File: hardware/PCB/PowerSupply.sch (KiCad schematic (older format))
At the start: 8 parts

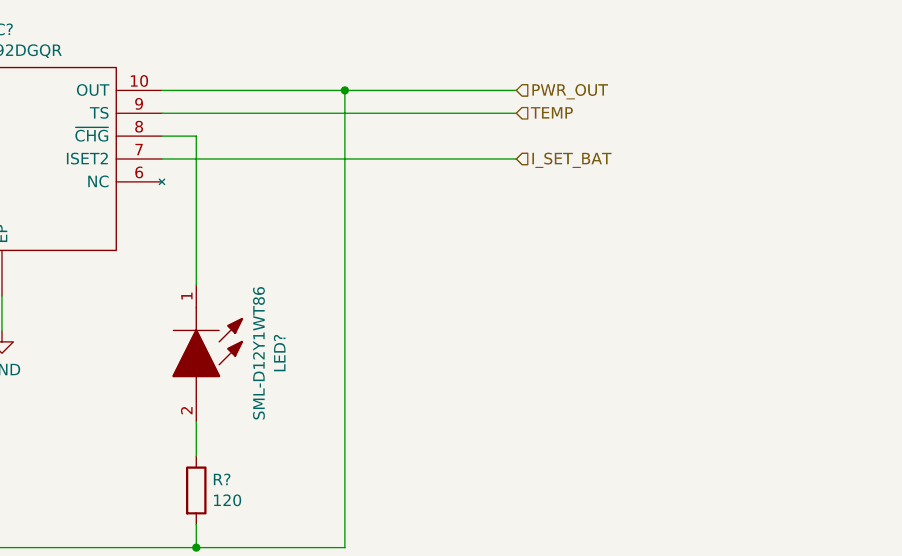
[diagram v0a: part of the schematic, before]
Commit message: Added battery connector
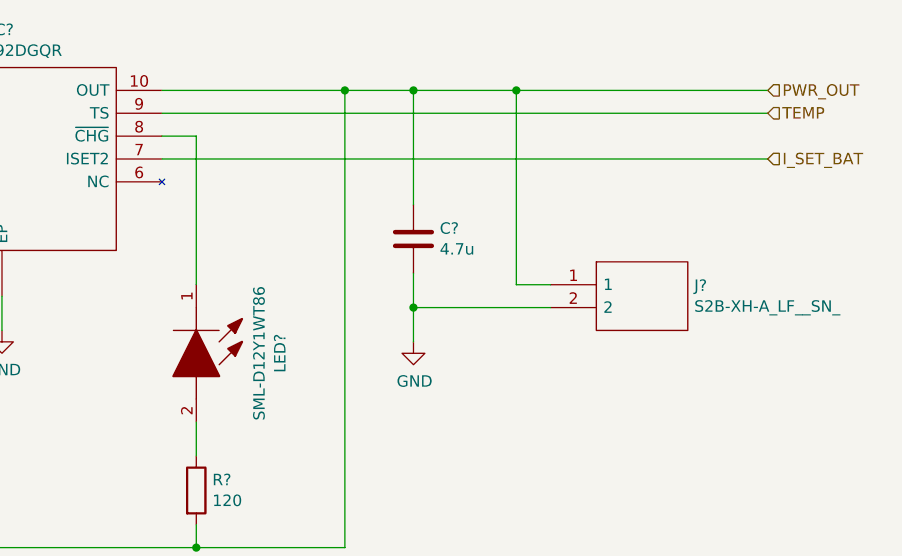
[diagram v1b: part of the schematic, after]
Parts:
- added C?: 4.7u, Capacitor_SMD:C_0603_1608Metric, symbol Device:C
- added J?: S2B-XH-A_LF__SN_, SHDRRA2W80P0X250_1X2_740X1150X610P, symbol ProjectLibrary:S2B-XH-A_LF__SN_
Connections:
- net GND: now also C?.2, J?.2
- net PWR_OUT: now also C?.1, J?.1
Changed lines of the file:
@@
 	1    0    0    -1
 $EndComp
-Text HLabel 6200 1650 2    50   Input ~ 0
+Text HLabel 7300 1650 2    50   Input ~ 0
 I_SET_BAT
-Text HLabel 6200 1450 2    50   Input ~ 0
+Text HLabel 7300 1450 2    50   Input ~ 0
 TEMP
 Wire Wire Line
@@
 Wire Wire Line
 	4650 1550 4800 1550
-Text HLabel 6200 1350 2    50   Input ~ 0
+Text HLabel 7300 1350 2    50   Input ~ 0
 PWR_OUT
 $Comp
@@
 Connection ~ 5450 1350
 Wire Wire Line
-	5450 1350 6200 1350
+	5450 1350 5750 1350
 Wire Wire Line
 	4650 1350 5450 1350
-Wire Wire Line
-	4650 1450 6200 1450
-Wire Wire Line
-	4650 1650 6200 1650
 Wire Wire Line
 	3150 2200 3150 1750
@@
 Wire Wire Line
 	3950 2250 3950 2400
+$Comp
+L Device:C C?
+U 1 1 5FC2DE09
+P 5750 2000
+F 0 "C?" H 5865 2046 50  0000 L CNN
+F 1 "4.7u" H 5865 1955 50  0000 L CNN
+F 2 "Capacitor_SMD:C_0603_1608Metric" H 5788 1850 50  0001 C CNN
+F 3 "~" H 5750 2000 50  0001 C CNN
+	1    5750 2000
+	1    0    0    -1
+$EndComp
+$Comp
+L power:GND #PWR?
+U 1 1 5FC2E9CD
+P 5750 2450
+F 0 "#PWR?" H 5750 2200 50  0001 C CNN
+F 1 "GND" H 5755 2277 50  0000 C CNN
+F 2 "" H 5750 2450 50  0001 C CNN
+F 3 "" H 5750 2450 50  0001 C CNN
+	1    5750 2450
+	1    0    0    -1
+$EndComp
+Wire Wire Line
+	5750 2300 5750 2150
+Wire Wire Line
+	5750 1850 5750 1350
+Connection ~ 5750 1350
+Wire Wire Line
+	5750 1350 6200 1350
+$Comp
+L ProjectLibrary:S2B-XH-A_LF__SN_ J?
+U 1 1 5FC2F7E2
+P 6350 2200
+F 0 "J?" H 6978 2196 50  0000 L CNN
+F 1 "S2B-XH-A_LF__SN_" H 6978 2105 50  0000 L CNN
+F 2 "SHDRRA2W80P0X250_1X2_740X1150X610P" H 7000 2300 50  0001 L CNN
+F 3 "http://www.jst-mfg.com/product/pdf/eng/eXH.pdf" H 7000 2200 50  0001 L CNN
+F 4 "XH-2.5mm Header side entry 2 way JST XH Series, Series Number S2B, 2.5mm Pitch 2 Way 1 Row Right Angle PCB Header, Solder Termination, 3A" H 7000 2100 50  0001 L CNN "Description"
+F 5 "6.1" H 7000 2000 50  0001 L CNN "Height"
+F 6 "JST (JAPAN SOLDERLESS TERMINALS)" H 7000 1900 50  0001 L CNN "Manufacturer_Name"
+F 7 "S2B-XH-A(LF)(SN)" H 7000 1800 50  0001 L CNN "Manufacturer_Part_Number"
+F 8 "S2B-XH-A(LF)(SN)" H 7000 1700 50  0001 L CNN "Arrow Part Number"
+F 9 "https://www.arrow.com/en/products/s2b-xh-a-lf-sn/jst-manufacturing" H 7000 1600 50  0001 L CNN "Arrow Price/Stock"
+F 10 "" H 7000 1500 50  0001 L CNN "Mouser Part Number"
+F 11 "" H 7000 1400 50  0001 L CNN "Mouser Price/Stock"
+	1    6350 2200
+	1    0    0    -1
+$EndComp
+Wire Wire Line
+	6350 2300 5750 2300
+Wire Wire Line
+	5750 2300 5750 2450
+Connection ~ 5750 2300
+Wire Wire Line
+	4650 1650 7300 1650
+Wire Wire Line
+	4650 1450 7300 1450
+Wire Wire Line
+	6350 2200 6200 2200
+Wire Wire Line
+	6200 2200 6200 1350
+Wire Wire Line
+	6200 1350 7300 1350
+Connection ~ 6200 1350
 $EndSCHEMATC

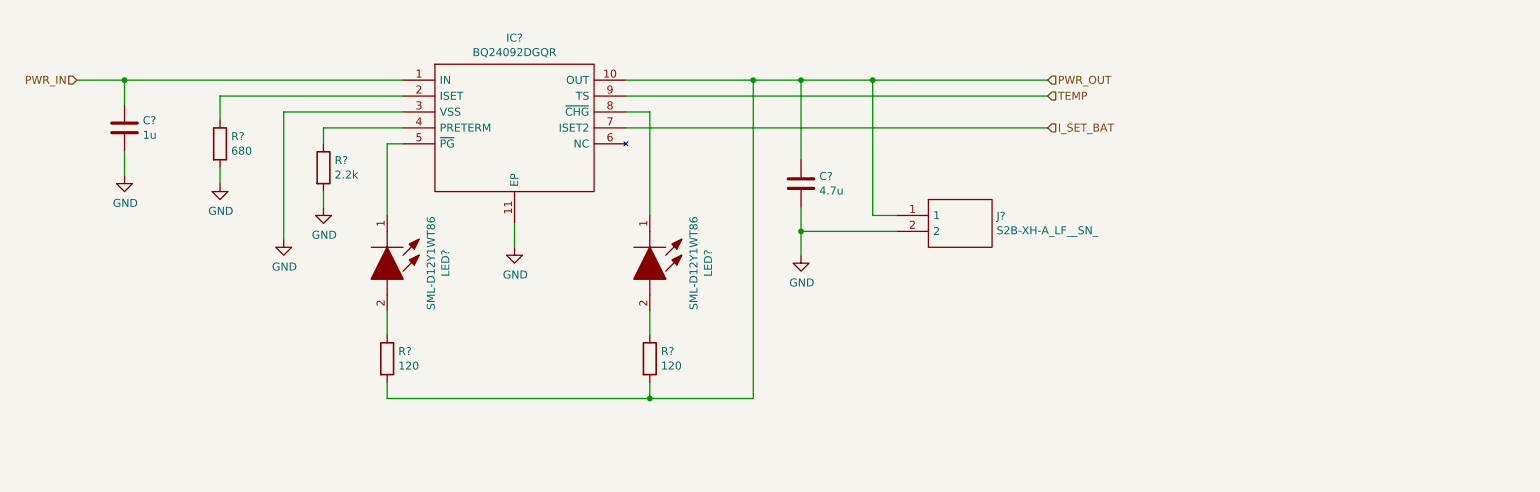
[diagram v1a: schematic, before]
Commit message: Add TPS62290DRV to PowerSupply
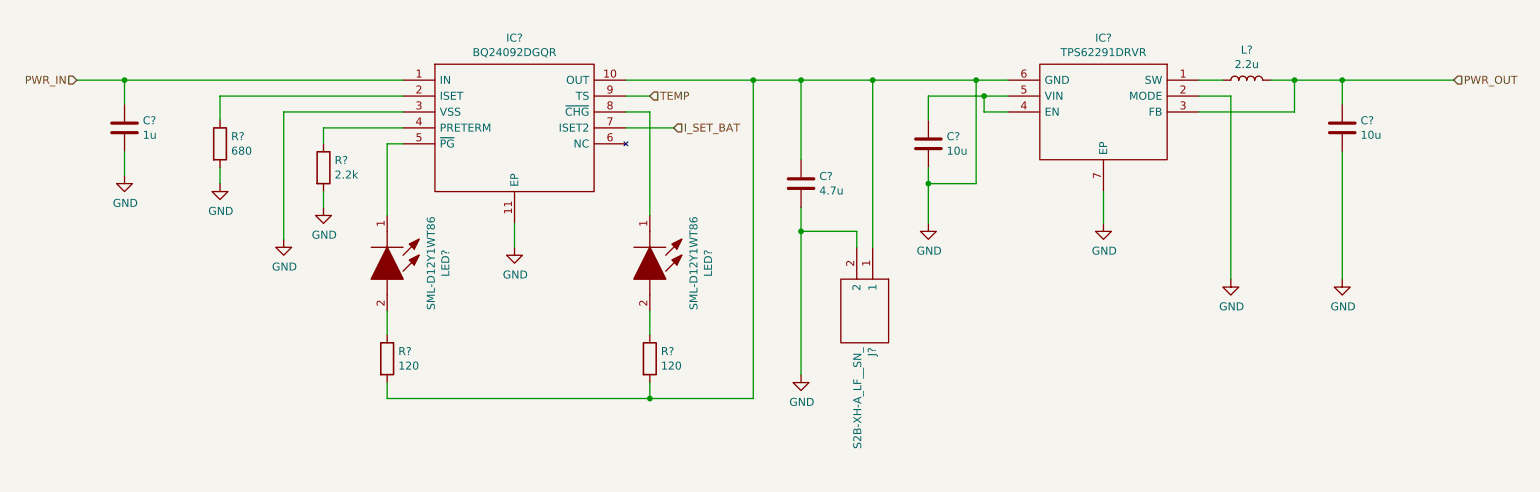
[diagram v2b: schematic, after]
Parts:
- added C? (x2): 10u, symbol Device:C
- added IC?: TPS62291DRVR, SON65P200X200X80-7N, symbol ProjectLibrary:TPS62291DRVR
- added L?: 2.2u, symbol Device:L
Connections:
- net GND: now also C?.1, IC?.10 (OUT), J?.1, R?.2, R?.2, C?.2, C?.2, IC?.2 (MODE), IC?.6 (GND), IC?.7 (EP)
- net PWR_OUT: now also C?.1, IC?.3 (FB), L?.2; no longer C?.1, IC?.10 (OUT), J?.1, R?.2, R?.2
- new net: IC?.1 (SW), L?.1
- new net: C?.1, IC?.4 (EN), IC?.5 (VIN)
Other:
- moved on the sheet: J?
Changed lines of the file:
@@
 	1    0    0    -1
 $EndComp
-Text HLabel 7300 1650 2    50   Input ~ 0
+Text HLabel 4950 1650 2    50   Input ~ 0
 I_SET_BAT
-Text HLabel 7300 1450 2    50   Input ~ 0
+Text HLabel 4800 1450 2    50   Input ~ 0
 TEMP
 Wire Wire Line
@@
 Wire Wire Line
 	4650 1550 4800 1550
-Text HLabel 7300 1350 2    50   Input ~ 0
+Text HLabel 9850 1350 2    50   Input ~ 0
 PWR_OUT
 $Comp
@@
 L power:GND #PWR?
 U 1 1 5FC2E9CD
-P 5750 2450
-F 0 "#PWR?" H 5750 2200 50  0001 C CNN
-F 1 "GND" H 5755 2277 50  0000 C CNN
-F 2 "" H 5750 2450 50  0001 C CNN
-F 3 "" H 5750 2450 50  0001 C CNN
-	1    5750 2450
-	1    0    0    -1
-$EndComp
-Wire Wire Line
-	5750 2300 5750 2150
+P 5750 3200
+F 0 "#PWR?" H 5750 2950 50  0001 C CNN
+F 1 "GND" H 5755 3027 50  0000 C CNN
+F 2 "" H 5750 3200 50  0001 C CNN
+F 3 "" H 5750 3200 50  0001 C CNN
+	1    5750 3200
+	1    0    0    -1
+$EndComp
 Wire Wire Line
 	5750 1850 5750 1350
@@
 L ProjectLibrary:S2B-XH-A_LF__SN_ J?
 U 1 1 5FC2F7E2
-P 6350 2200
-F 0 "J?" H 6978 2196 50  0000 L CNN
-F 1 "S2B-XH-A_LF__SN_" H 6978 2105 50  0000 L CNN
-F 2 "SHDRRA2W80P0X250_1X2_740X1150X610P" H 7000 2300 50  0001 L CNN
-F 3 "http://www.jst-mfg.com/product/pdf/eng/eXH.pdf" H 7000 2200 50  0001 L CNN
-F 4 "XH-2.5mm Header side entry 2 way JST XH Series, Series Number S2B, 2.5mm Pitch 2 Way 1 Row Right Angle PCB Header, Solder Termination, 3A" H 7000 2100 50  0001 L CNN "Description"
-F 5 "6.1" H 7000 2000 50  0001 L CNN "Height"
-F 6 "JST (JAPAN SOLDERLESS TERMINALS)" H 7000 1900 50  0001 L CNN "Manufacturer_Name"
-F 7 "S2B-XH-A(LF)(SN)" H 7000 1800 50  0001 L CNN "Manufacturer_Part_Number"
-F 8 "S2B-XH-A(LF)(SN)" H 7000 1700 50  0001 L CNN "Arrow Part Number"
-F 9 "https://www.arrow.com/en/products/s2b-xh-a-lf-sn/jst-manufacturing" H 7000 1600 50  0001 L CNN "Arrow Price/Stock"
-F 10 "" H 7000 1500 50  0001 L CNN "Mouser Part Number"
-F 11 "" H 7000 1400 50  0001 L CNN "Mouser Price/Stock"
-	1    6350 2200
-	1    0    0    -1
-$EndComp
-Wire Wire Line
-	6350 2300 5750 2300
-Wire Wire Line
-	5750 2300 5750 2450
+P 6200 2400
+F 0 "J?" H 6828 2396 50  0000 L CNN
+F 1 "S2B-XH-A_LF__SN_" H 6828 2305 50  0000 L CNN
+F 2 "SHDRRA2W80P0X250_1X2_740X1150X610P" H 6850 2500 50  0001 L CNN
+F 3 "http://www.jst-mfg.com/product/pdf/eng/eXH.pdf" H 6850 2400 50  0001 L CNN
+F 4 "XH-2.5mm Header side entry 2 way JST XH Series, Series Number S2B, 2.5mm Pitch 2 Way 1 Row Right Angle PCB Header, Solder Termination, 3A" H 6850 2300 50  0001 L CNN "Description"
+F 5 "6.1" H 6850 2200 50  0001 L CNN "Height"
+F 6 "JST (JAPAN SOLDERLESS TERMINALS)" H 6850 2100 50  0001 L CNN "Manufacturer_Name"
+F 7 "S2B-XH-A(LF)(SN)" H 6850 2000 50  0001 L CNN "Manufacturer_Part_Number"
+F 8 "S2B-XH-A(LF)(SN)" H 6850 1900 50  0001 L CNN "Arrow Part Number"
+F 9 "https://www.arrow.com/en/products/s2b-xh-a-lf-sn/jst-manufacturing" H 6850 1800 50  0001 L CNN "Arrow Price/Stock"
+F 10 "" H 6850 1700 50  0001 L CNN "Mouser Part Number"
+F 11 "" H 6850 1600 50  0001 L CNN "Mouser Price/Stock"
+	1    6200 2400
+	0    1    1    0
+$EndComp
+$Comp
+L ProjectLibrary:TPS62291DRVR IC?
+U 1 1 5FC09EEE
+P 8250 1350
+F 0 "IC?" H 8850 1615 50  0000 C CNN
+F 1 "TPS62291DRVR" H 8850 1524 50  0000 C CNN
+F 2 "SON65P200X200X80-7N" H 9300 1450 50  0001 L CNN
+F 3 "https://componentsearchengine.com/ga/detail.html?searchString=TPS62291DRVR&manuf=Texas%20Instruments&country=US&language=en&source=63" H 9300 1350 50  0001 L CNN
+F 4 "Voltage Regulators - Switching Regulators 2.25MHz 1A Step-Down Converter" H 9300 1250 50  0001 L CNN "Description"
+F 5 "0.8" H 9300 1150 50  0001 L CNN "Height"
+F 6 "595-TPS62291DRVR" H 9300 1050 50  0001 L CNN "Mouser Part Number"
+F 7 "https://www.mouser.co.uk/ProductDetail/Texas-Instruments/TPS62291DRVR?qs=WxL8HmPi5r5oemxPY8jLwQ%3D%3D" H 9300 950 50  0001 L CNN "Mouser Price/Stock"
+F 8 "Texas Instruments" H 9300 850 50  0001 L CNN "Manufacturer_Name"
+F 9 "TPS62291DRVR" H 9300 750 50  0001 L CNN "Manufacturer_Part_Number"
+	1    8250 1350
+	-1   0    0    -1
+$EndComp
+$Comp
+L power:GND #PWR?
+U 1 1 5FC12B1D
+P 6550 2250
+F 0 "#PWR?" H 6550 2000 50  0001 C CNN
+F 1 "GND" H 6555 2077 50  0000 C CNN
+F 2 "" H 6550 2250 50  0001 C CNN
+F 3 "" H 6550 2250 50  0001 C CNN
+	1    6550 2250
+	1    0    0    -1
+$EndComp
+$Comp
+L Device:C C?
+U 1 1 5FC139FA
+P 6550 1750
+F 0 "C?" H 6665 1796 50  0000 L CNN
+F 1 "10u" H 6665 1705 50  0000 L CNN
+F 2 "" H 6588 1600 50  0001 C CNN
+F 3 "~" H 6550 1750 50  0001 C CNN
+	1    6550 1750
+	1    0    0    -1
+$EndComp
+Wire Wire Line
+	6550 2250 6550 2000
+Wire Wire Line
+	6550 1600 6550 1450
+Wire Wire Line
+	6550 1450 6900 1450
+Wire Wire Line
+	7050 1350 6850 1350
+Wire Wire Line
+	6850 1350 6850 2000
+Wire Wire Line
+	6850 2000 6550 2000
+Connection ~ 6550 2000
+Wire Wire Line
+	6550 2000 6550 1900
+Wire Wire Line
+	7050 1550 6900 1550
+Wire Wire Line
+	6900 1550 6900 1450
+Connection ~ 6900 1450
+Wire Wire Line
+	6900 1450 7050 1450
+Wire Wire Line
+	8250 1450 8450 1450
+$Comp
+L power:GND #PWR?
+U 1 1 5FC1A4A2
+P 8450 2600
+F 0 "#PWR?" H 8450 2350 50  0001 C CNN
+F 1 "GND" H 8455 2427 50  0000 C CNN
+F 2 "" H 8450 2600 50  0001 C CNN
+F 3 "" H 8450 2600 50  0001 C CNN
+	1    8450 2600
+	1    0    0    -1
+$EndComp
+$Comp
+L power:GND #PWR?
+U 1 1 5FC1D2CA
+P 7650 2250
+F 0 "#PWR?" H 7650 2000 50  0001 C CNN
+F 1 "GND" H 7655 2077 50  0000 C CNN
+F 2 "" H 7650 2250 50  0001 C CNN
+F 3 "" H 7650 2250 50  0001 C CNN
+	1    7650 2250
+	1    0    0    -1
+$EndComp
+Wire Wire Line
+	7650 2050 7650 2250
+$Comp
+L Device:L L?
+U 1 1 5FC1EB27
+P 8550 1350
+F 0 "L?" V 8740 1350 50  0000 C CNN
+F 1 "2.2u" V 8649 1350 50  0000 C CNN
+F 2 "" H 8550 1350 50  0001 C CNN
+F 3 "~" H 8550 1350 50  0001 C CNN
+	1    8550 1350
+	0    -1   -1   0
+$EndComp
+Wire Wire Line
+	8250 1350 8400 1350
+$Comp
+L Device:C C?
+U 1 1 5FC33F95
+P 9150 1650
+F 0 "C?" H 9265 1696 50  0000 L CNN
+F 1 "10u" H 9265 1605 50  0000 L CNN
+F 2 "" H 9188 1500 50  0001 C CNN
+F 3 "~" H 9150 1650 50  0001 C CNN
+	1    9150 1650
+	1    0    0    -1
+$EndComp
+Wire Wire Line
+	4650 1450 4800 1450
+Wire Wire Line
+	4950 1650 4650 1650
+Wire Wire Line
+	5750 2150 5750 2300
+Wire Wire Line
+	6200 1350 6200 2400
+Wire Wire Line
+	6100 2400 6100 2300
+Wire Wire Line
+	6100 2300 5750 2300
 Connection ~ 5750 2300
 Wire Wire Line
-	4650 1650 7300 1650
-Wire Wire Line
-	4650 1450 7300 1450
-Wire Wire Line
-	6350 2200 6200 2200
-Wire Wire Line
-	6200 2200 6200 1350
-Wire Wire Line
-	6200 1350 7300 1350
+	5750 2300 5750 3200
+Wire Wire Line
+	6850 1350 6200 1350
+Connection ~ 6850 1350
 Connection ~ 6200 1350
+Wire Wire Line
+	9150 1500 9150 1350
+$Comp
+L power:GND #PWR?
+U 1 1 5FC4D9AD
+P 9150 2600
+F 0 "#PWR?" H 9150 2350 50  0001 C CNN
+F 1 "GND" H 9155 2427 50  0000 C CNN
+F 2 "" H 9150 2600 50  0001 C CNN
+F 3 "" H 9150 2600 50  0001 C CNN
+	1    9150 2600
+	1    0    0    -1
+$EndComp
+Wire Wire Line
+	9150 2600 9150 1800
+Wire Wire Line
+	8700 1350 8850 1350
+Wire Wire Line
+	8450 1450 8450 2600
+Wire Wire Line
+	8850 1550 8850 1350
+Wire Wire Line
+	8250 1550 8850 1550
+Connection ~ 8850 1350
+Wire Wire Line
+	8850 1350 9150 1350
+Connection ~ 9150 1350
+Wire Wire Line
+	9150 1350 9850 1350
 $EndSCHEMATC
